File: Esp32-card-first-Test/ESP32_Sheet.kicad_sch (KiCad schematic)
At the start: 2 parts, among them J1 Conn_01x14_Socket

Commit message: .
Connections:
- net 3v3: now also J1.14 (Pin_14)
- net GND: now also J1.13 (Pin_13)
- net at J1.10 (Pin_10): now also ESP32_WROOM_KIT1.32 (GPIO4)
- net at J1.11 (Pin_11): now also ESP32_WROOM_KIT1.22 (GPIO22)
- net at J1.12 (Pin_12): now also ESP32_WROOM_KIT1.29 (GPIO5)
- net at J1.6 (Pin_6): now also ESP32_WROOM_KIT1.27 (GPIO19)
- net at J1.7 (Pin_7): now also ESP32_WROOM_KIT1.35 (GPIO15)
- net at J1.8 (Pin_8): now also ESP32_WROOM_KIT1.28 (GPIO18)
- net at J1.9 (Pin_9): now also ESP32_WROOM_KIT1.21 (GPIO23)
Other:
- moved on the sheet: J1

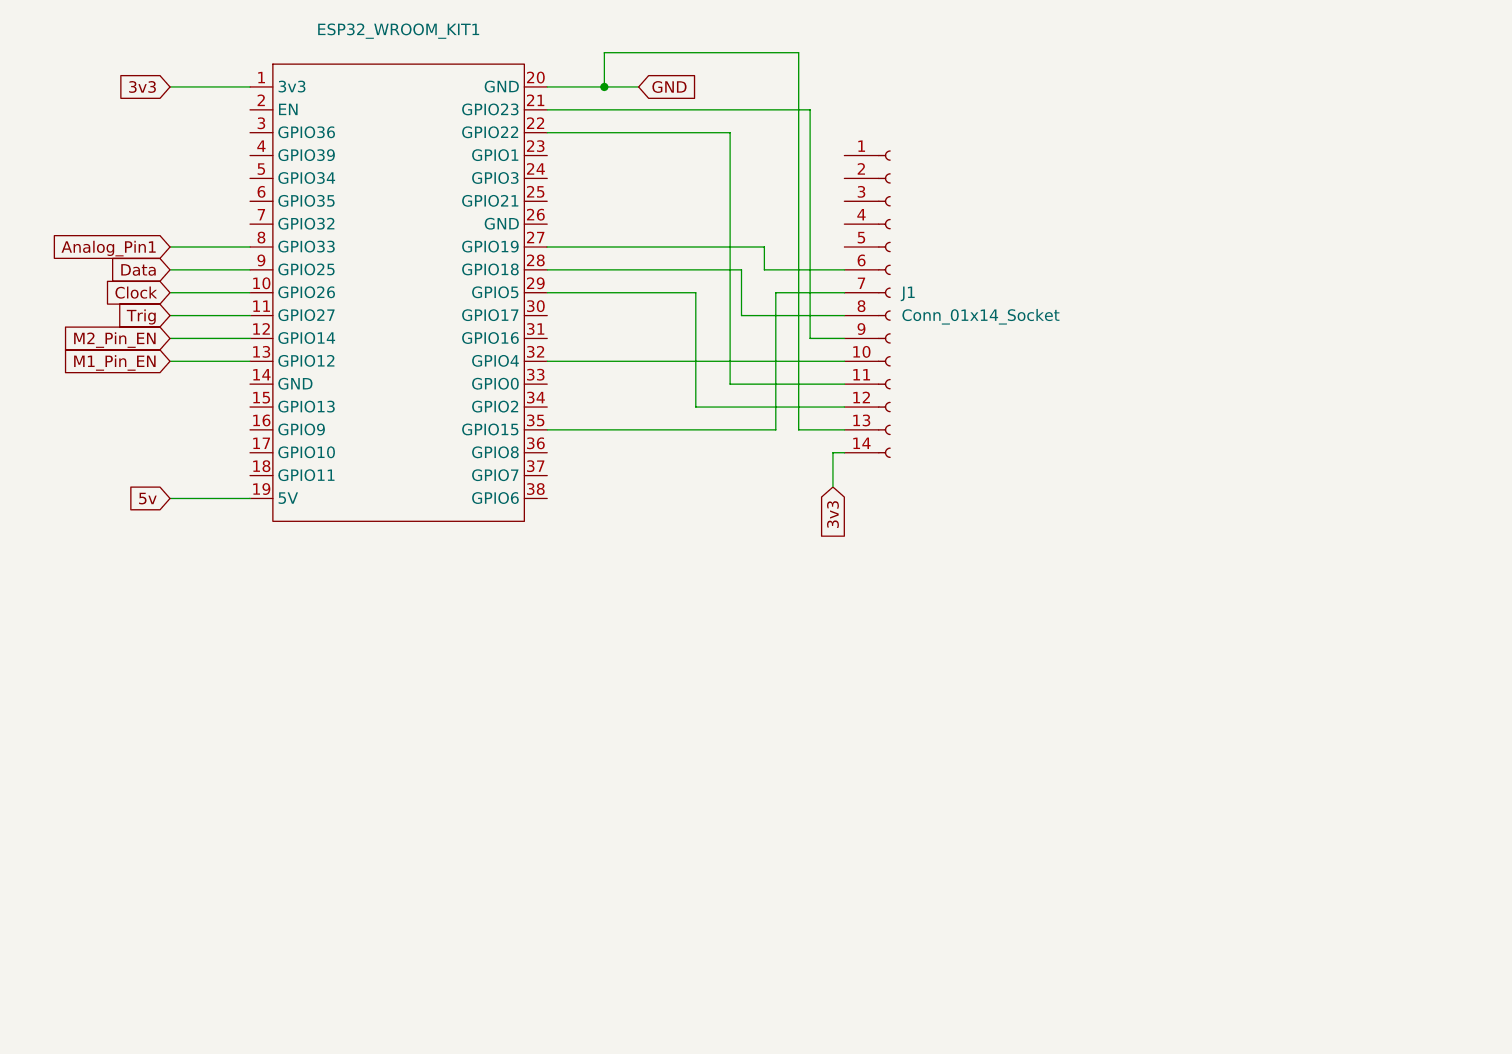
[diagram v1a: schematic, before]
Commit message: add and congif Visual studio code projet
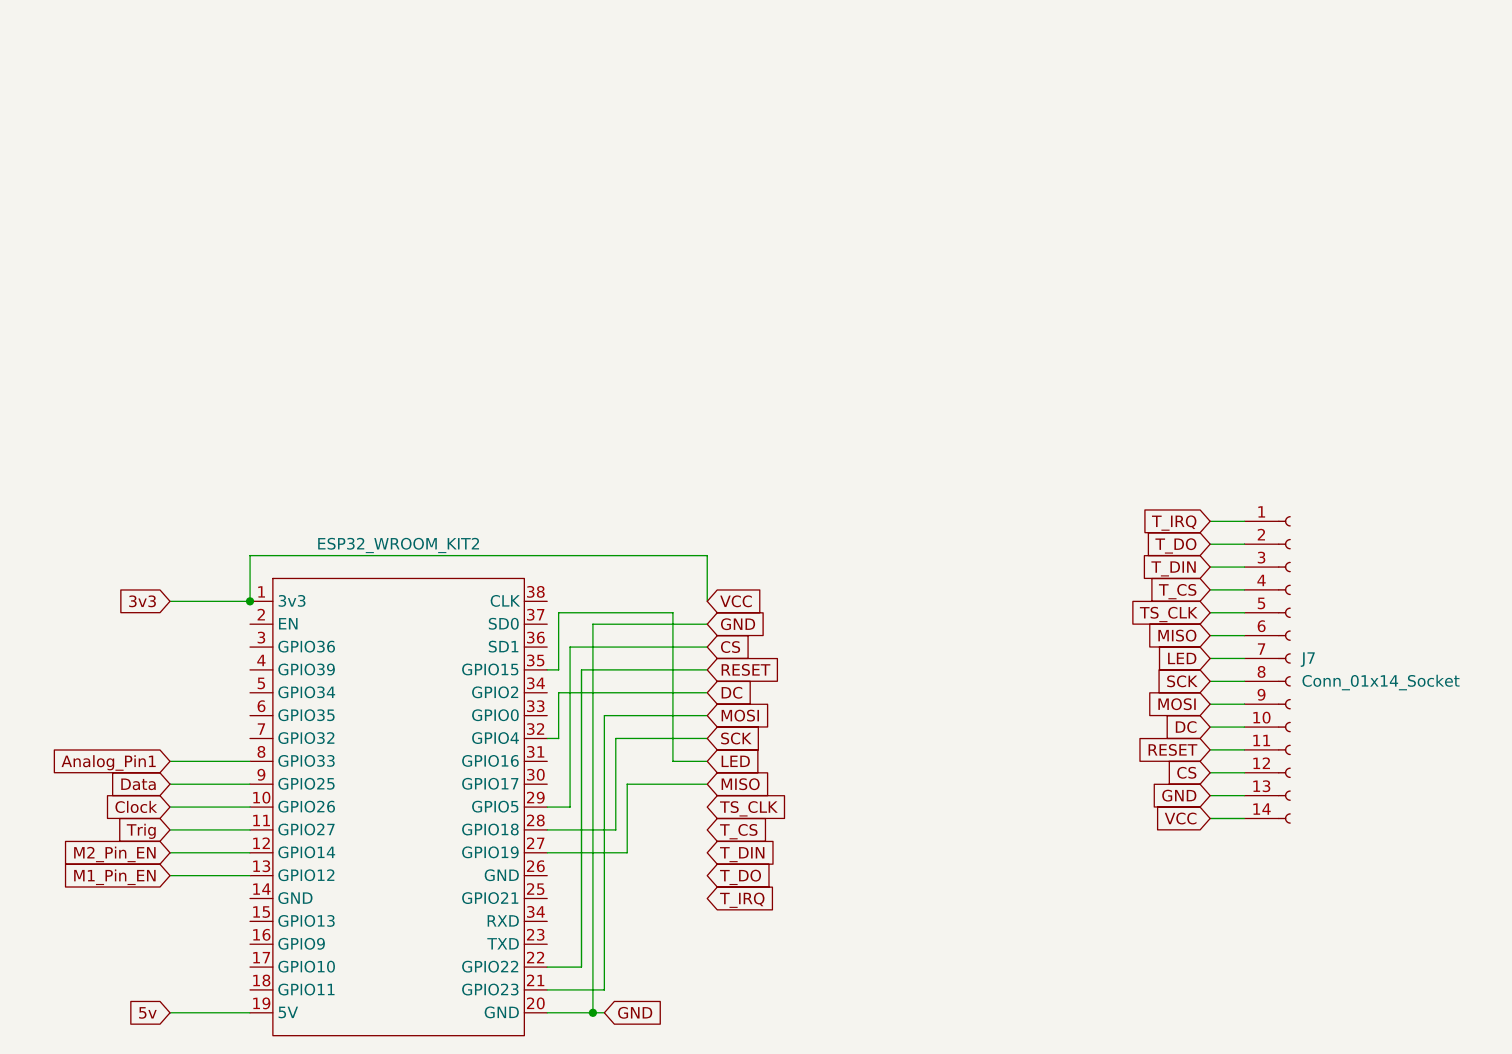
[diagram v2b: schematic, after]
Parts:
- removed ESP32_WROOM_KIT1: ~, MyEsp32Library:Esp32_Wroom32_DevKit, symbol MyEsp32_Library:Esp32_38pin
- removed J1: Conn_01x14_Socket, Connector_PinSocket_2.54mm:PinSocket_1x14_P2.54mm_Vertical, symbol Connector:Conn_01x14_Socket
- added ESP32_WROOM_KIT2: ~, MyEsp32Library:Esp32_Wroom32_DevKit, symbol MyEsp32_Library:Esp32_38pin
- added J7: Conn_01x14_Socket, Connector_PinSocket_2.54mm:PinSocket_1x14_P2.54mm_Vertical, symbol Connector:Conn_01x14_Socket
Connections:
- net 3v3: now also ESP32_WROOM_KIT2.1 (3v3), J7.14 (Pin_14)
- net 5v: now also ESP32_WROOM_KIT2.19 (5V)
- net Analog_Pin1: now also ESP32_WROOM_KIT2.8 (GPIO33)
- net Clock: now also ESP32_WROOM_KIT2.10 (GPIO26)
- net Data: now also ESP32_WROOM_KIT2.9 (GPIO25)
- net GND: now also ESP32_WROOM_KIT2.20 (GND), J7.13 (Pin_13)
- net M1_Pin_EN: now also ESP32_WROOM_KIT2.13 (GPIO12)
- net M2_Pin_EN: now also ESP32_WROOM_KIT2.12 (GPIO14)
- net Trig: now also ESP32_WROOM_KIT2.11 (GPIO27)
- new net CS: ESP32_WROOM_KIT2.29 (GPIO5), J7.12 (Pin_12)
- new net DC: ESP32_WROOM_KIT2.32 (GPIO4), J7.10 (Pin_10)
- new net LED: ESP32_WROOM_KIT2.35 (GPIO15), J7.7 (Pin_7)
- new net MISO: ESP32_WROOM_KIT2.27 (GPIO19), J7.6 (Pin_6)
- new net MOSI: ESP32_WROOM_KIT2.21 (GPIO23), J7.9 (Pin_9)
- new net RESET: ESP32_WROOM_KIT2.22 (GPIO22), J7.11 (Pin_11)
- new net SCK: ESP32_WROOM_KIT2.28 (GPIO18), J7.8 (Pin_8)
- new net TS_CLK: J7.5 (Pin_5)
- new net T_CS: J7.4 (Pin_4)
- new net T_DIN: J7.3 (Pin_3)
- new net T_DO: J7.2 (Pin_2)
- new net T_IRQ: J7.1 (Pin_1)
